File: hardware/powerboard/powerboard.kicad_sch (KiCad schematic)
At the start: 64 parts, among them J1 USB_B_Micro, J2 Boot, J3 Power, J4 SPI_0, J5 Debug, J6 SPI_1, J7 I2C_0, J8 I2C_1, J9 UART_0, SW1 Oct_Up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

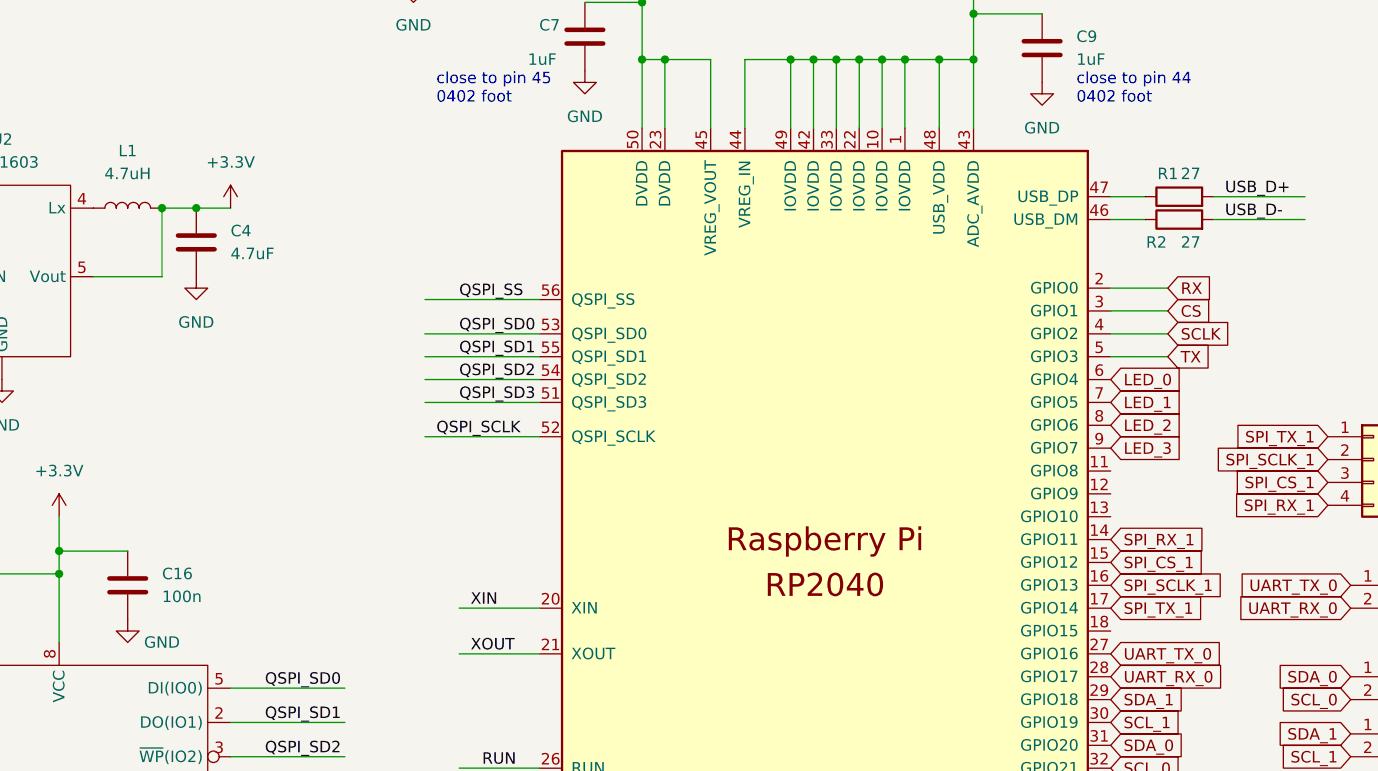
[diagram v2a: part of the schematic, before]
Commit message: GPIO Functions done Small footprint changes to powerboard
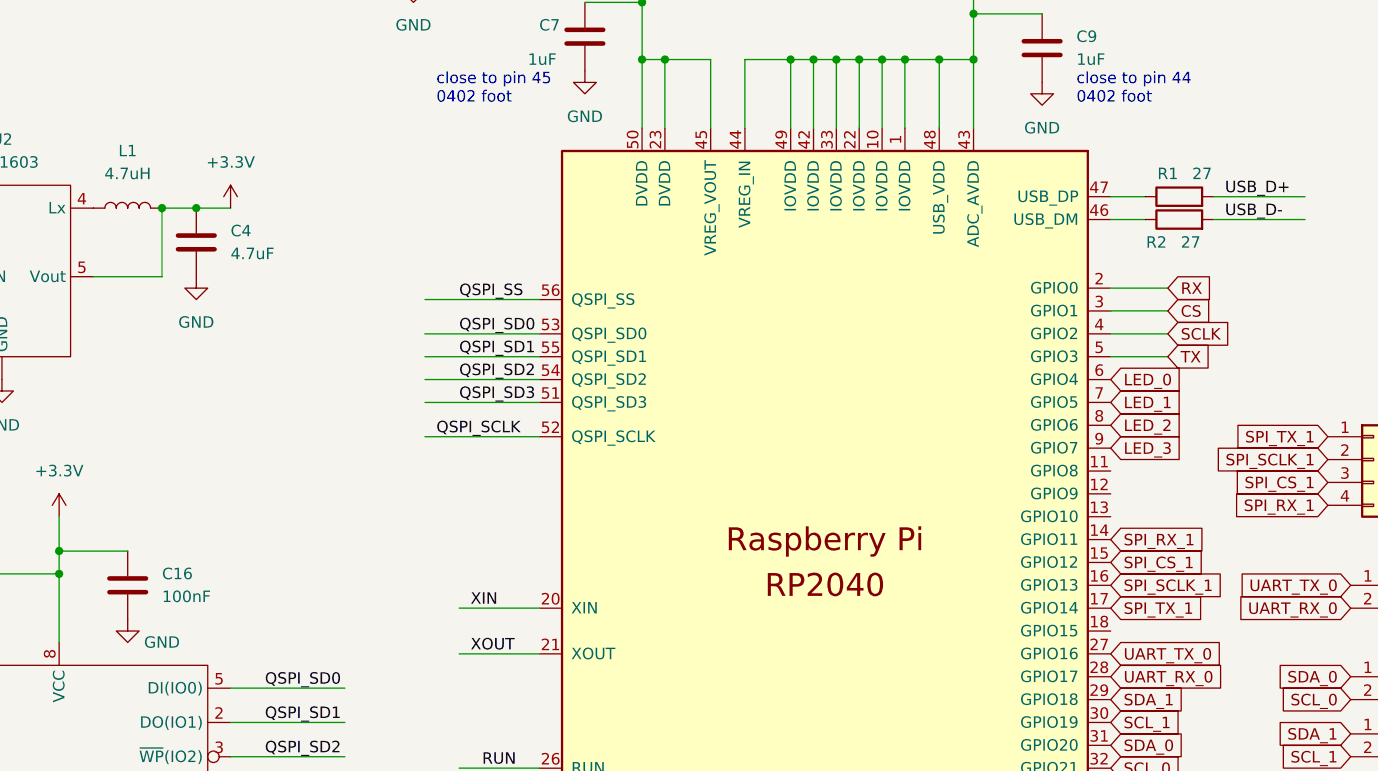
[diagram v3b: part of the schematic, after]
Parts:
- C16: value 100n -> 100nF
- C22: footprint Capacitor_SMD:C_0603_1608Metric -> Capacitor_SMD:C_0805_2012Metric
- C23, C24: footprint Capacitor_SMD:C_0603_1608Metric -> Capacitor_SMD:C_0402_1005Metric
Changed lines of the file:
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@@
     (in_bom yes) (on_board yes)
     (property "Reference" "R1" (id 0) (at 196.85 58.42 90))
-    (property "Value" "27" (id 1) (at 199.39 58.42 90))
+    (property "Value" "27" (id 1) (at 200.66 58.42 90))
     (property "Footprint" "Resistor_SMD:R_0402_1005Metric" (id 2) (at 198.12 62.738 90)
       (effects (font (size 1.27 1.27)) hide)
@@
       (effects (font (size 1.27 1.27)) (justify left))
     )
-    (property "Footprint" "Capacitor_SMD:C_0603_1608Metric" (id 2) (at 77.1652 194.31 0)
+    (property "Footprint" "Capacitor_SMD:C_0402_1005Metric" (id 2) (at 77.1652 194.31 0)
       (effects (font (size 1.27 1.27)) hide)
     )
@@
       (effects (font (size 1.27 1.27)) (justify left))
     )
-    (property "Value" "100n" (id 1) (at 85.09 105.4099 0)
+    (property "Value" "100nF" (id 1) (at 85.09 105.4099 0)
       (effects (font (size 1.27 1.27)) (justify left))
     )
@@
       (effects (font (size 1.27 1.27)) (justify left))
     )
-    (property "Footprint" "Capacitor_SMD:C_0603_1608Metric" (id 2) (at 87.3252 180.34 0)
+    (property "Footprint" "Capacitor_SMD:C_0402_1005Metric" (id 2) (at 87.3252 180.34 0)
       (effects (font (size 1.27 1.27)) hide)
     )
@@
       (effects (font (size 1.27 1.27)) (justify left))
     )
-    (property "Footprint" "Capacitor_SMD:C_0603_1608Metric" (id 2) (at 279.0952 67.31 0)
+    (property "Footprint" "Capacitor_SMD:C_0805_2012Metric" (id 2) (at 279.0952 67.31 0)
       (effects (font (size 1.27 1.27)) hide)
     )
@@
     )
     (path "/d94ce941-d973-4d50-9dcc-a718392ddb9d"
-      (reference "C16") (unit 1) (value "100n") (footprint "Capacitor_SMD:C_0603_1608Metric")
+      (reference "C16") (unit 1) (value "100nF") (footprint "Capacitor_SMD:C_0603_1608Metric")
     )
     (path "/17adefd0-27a9-46b5-ae61-8e173f9c410f"
@@
     )
     (path "/ea5ef4b8-1862-4679-b068-1d8aea36089c"
-      (reference "C22") (unit 1) (value "10u") (footprint "Capacitor_SMD:C_0603_1608Metric")
+      (reference "C22") (unit 1) (value "10u") (footprint "Capacitor_SMD:C_0805_2012Metric")
     )
     (path "/9cb838af-a4f1-4ad0-b52d-a490cbb33159"
-      (reference "C23") (unit 1) (value "100n") (footprint "Capacitor_SMD:C_0603_1608Metric")
+      (reference "C23") (unit 1) (value "100n") (footprint "Capacitor_SMD:C_0402_1005Metric")
     )
     (path "/e1581637-2922-404a-90ea-0fc41dfb0ff5"
-      (reference "C24") (unit 1) (value "100n") (footprint "Capacitor_SMD:C_0603_1608Metric")
+      (reference "C24") (unit 1) (value "100n") (footprint "Capacitor_SMD:C_0402_1005Metric")
     )
     (path "/f5fb7d56-553e-4b20-aeec-a8e1c9b6a666"

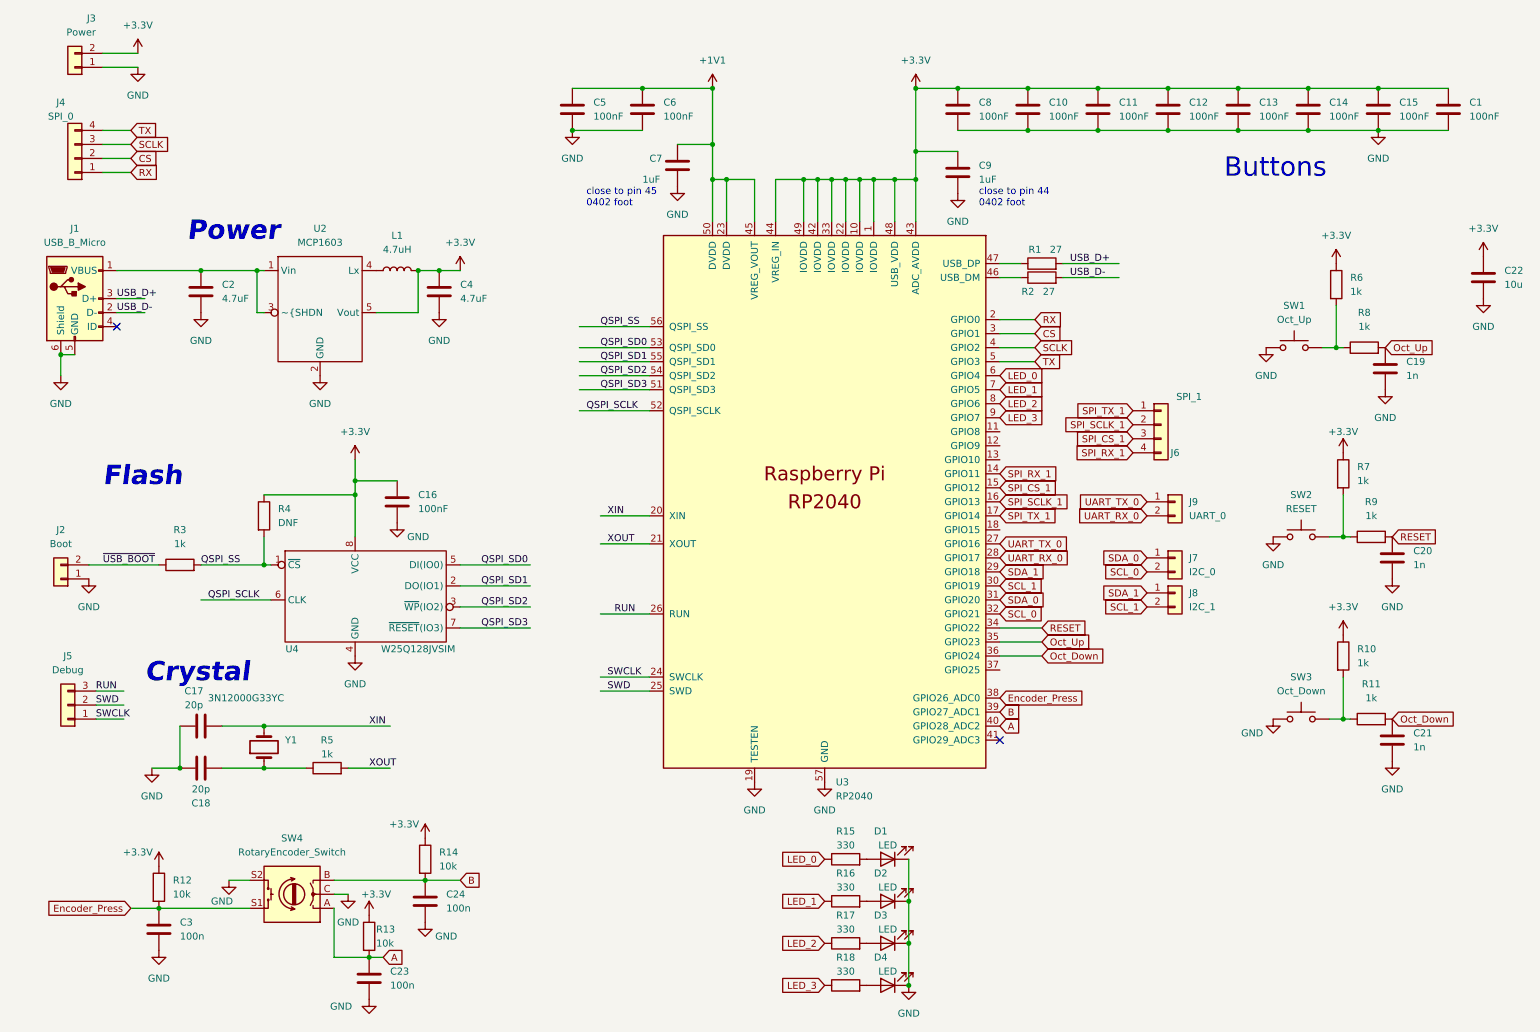
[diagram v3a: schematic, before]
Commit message: Powerboard Renovations (Stage 1 of Finalization)
Expand SPI 0 Header to match Display Header
Confirm footprints for passives
Power Circuit reorganized for short return paths
Reset button now toggles RUN pin, does not connect to GPIO
GPIO 10 connected to DISPLAY_RESET pin
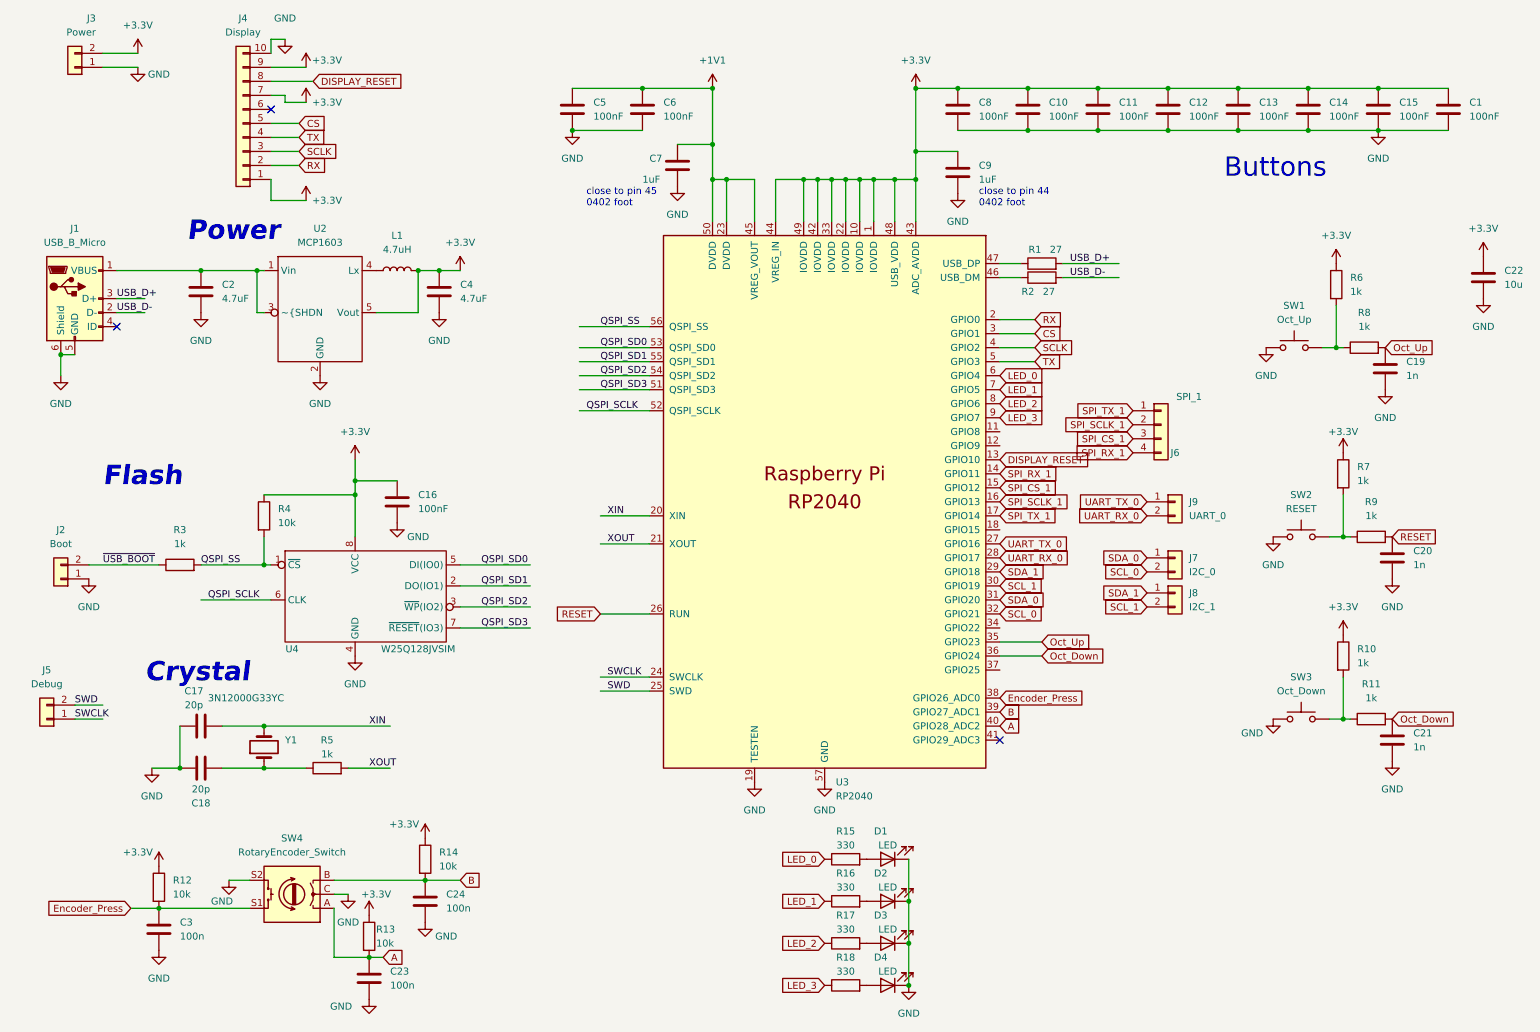
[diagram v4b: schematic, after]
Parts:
- removed J4: SPI_0, Connector_PinHeader_2.54mm:PinHeader_1x04_P2.54mm_Vertical, symbol Connector_Generic:Conn_01x04
- removed J5: Debug, Connector_PinHeader_2.54mm:PinHeader_1x03_P2.54mm_Vertical, symbol Connector_Generic:Conn_01x03
- added J4: Display, Connector_PinSocket_2.54mm:PinSocket_1x10_P2.54mm_Vertical, symbol Connector_Generic:Conn_01x10
- added J5: Debug, symbol Connector_Generic:Conn_01x02
- R4: value DNF -> 10k
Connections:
- net RUN is gone; now on net RESET: U3.26 (RUN)
- net +3.3V: now also J4.1 (Pin_1), J4.7 (Pin_7), J4.9 (Pin_9)
- net CS: now also J4.5 (Pin_5)
- net GND: now also J4.10 (Pin_10)
- net RESET: no longer U3.34 (GPIO22)
- net RX: now also J4.2 (Pin_2)
- net SCLK: now also J4.3 (Pin_3)
- net SWCLK: now also J5.1 (Pin_1)
- net SWD: now also J5.2 (Pin_2)
- net TX: now also J4.4 (Pin_4)
- net DISPLAY_RESET: now reaches U3.13 (GPIO10)
- net DISPLAY_RESET: now also J4.8 (Pin_8)
- no-connect marks 2 -> 3

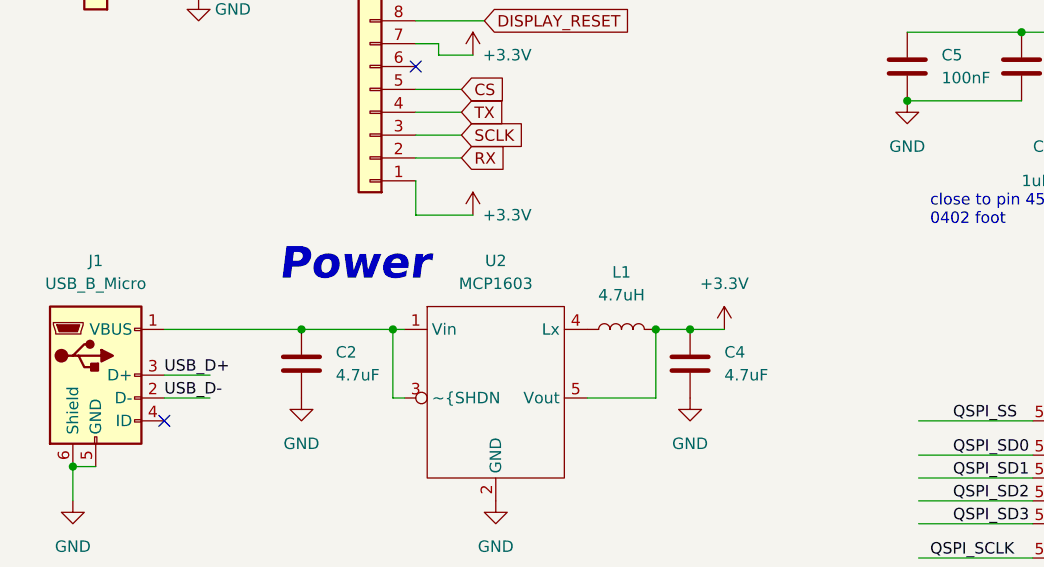
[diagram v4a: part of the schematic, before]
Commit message: Power Measurement Headers
Added, did not connect power measurement headers.
Do we need these?
How do we want to measure power?
This is a high current, high frequency path, can we even do a header like this?
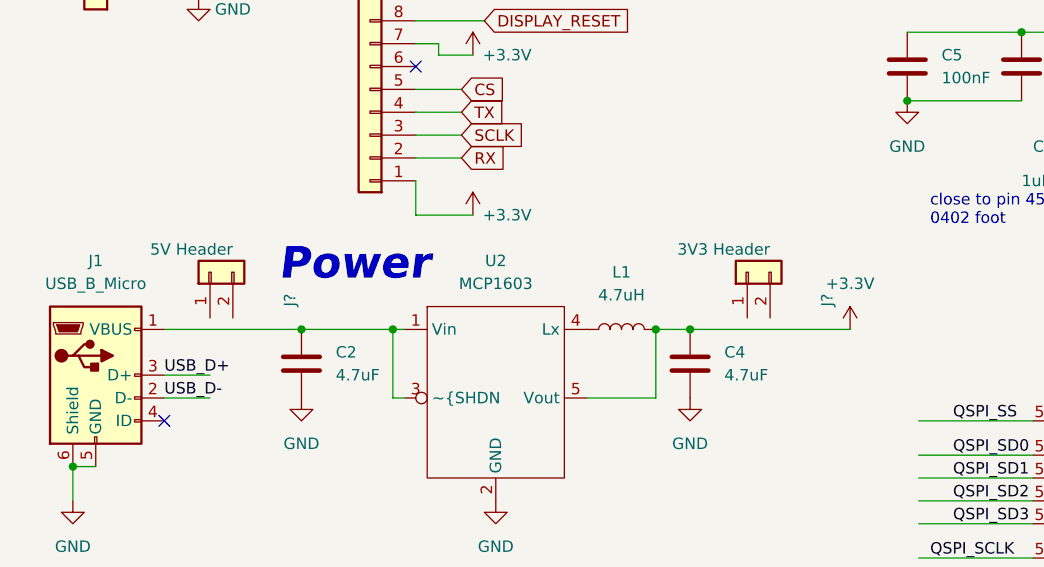
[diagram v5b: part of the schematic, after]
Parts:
- added J?: 5V Header, Connector_PinHeader_2.54mm:PinHeader_1x02_P2.54mm_Horizontal, symbol Connector_Generic:Conn_01x02
- added J?: 3V3 Header, Connector_PinHeader_2.54mm:PinHeader_1x02_P2.54mm_Horizontal, symbol Connector_Generic:Conn_01x02
- J5: footprint (none) -> Connector_PinSocket_2.54mm:PinSocket_1x02_P2.54mm_Vertical
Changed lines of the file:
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@@
     (stroke (width 0) (type default) (color 0 0 0 0))
   )
-  (wire (pts (xy 88.9 62.23) (xy 92.71 62.23))
+  (wire (pts (xy 88.9 62.23) (xy 106.68 62.23))
     (stroke (width 0) (type default) (color 0 0 0 0))
   )
@@
     (pin "2")
   )
+  (symbol (lib_id "Connector_Generic:Conn_01x02") (at 35.56 55.88 90) (unit 1)
+    (in_bom yes) (on_board yes)
+    (property "Reference" "J?" (id 0) (at 44.45 59.69 0)
+      (effects (font (size 1.27 1.27)) (justify left))
+    )
+    (property "Value" "5V Header" (id 1) (at 38.1 53.34 90)
+      (effects (font (size 1.27 1.27)) (justify left))
+    )
+    (property "Footprint" "Connector_PinHeader_2.54mm:PinHeader_1x02_P2.54mm_Horizontal" (id 2) (at 35.56 55.88 0)
+      (effects (font (size 1.27 1.27)) hide)
+    )
+    (property "Datasheet" "~" (id 3) (at 35.56 55.88 0)
+      (effects (font (size 1.27 1.27)) hide)
+    )
+    (pin "1")
+    (pin "2")
+  )
   (symbol (lib_id "Device:LED") (at 170.18 184.15 180) (unit 1)
     (in_bom yes) (on_board yes)
@@
     (pin "1")
   )
+  (symbol (lib_id "Connector_Generic:Conn_01x02") (at 95.25 55.88 90) (unit 1)
+    (in_bom yes) (on_board yes)
+    (property "Reference" "J?" (id 0) (at 104.14 59.69 0)
+      (effects (font (size 1.27 1.27)) (justify left))
+    )
+    (property "Value" "3V3 Header" (id 1) (at 97.79 53.34 90)
+      (effects (font (size 1.27 1.27)) (justify left))
+    )
+    (property "Footprint" "Connector_PinHeader_2.54mm:PinHeader_1x02_P2.54mm_Horizontal" (id 2) (at 95.25 55.88 0)
+      (effects (font (size 1.27 1.27)) hide)
+    )
+    (property "Datasheet" "~" (id 3) (at 95.25 55.88 0)
+      (effects (font (size 1.27 1.27)) hide)
+    )
+    (pin "1")
+    (pin "2")
+  )
   (symbol (lib_id "Device:R") (at 86.36 168.91 0) (unit 1)
     (in_bom yes) (on_board yes) (fields_autoplaced)
@@
     (property "Reference" "J5" (id 0) (at 17.78 134.62 0))
     (property "Value" "Debug" (id 1) (at 17.78 137.16 0))
-    (property "Footprint" "" (id 2) (at 17.78 143.51 0)
+    (property "Footprint" "Connector_PinSocket_2.54mm:PinSocket_1x02_P2.54mm_Vertical" (id 2) (at 17.78 143.51 0)
       (effects (font (size 1.27 1.27)) hide)
     )
@@
     (pin "2")
   )
-  (symbol (lib_id "power:+3.3V") (at 92.71 62.23 0) (unit 1)
-    (in_bom yes) (on_board yes) (fields_autoplaced)
-    (property "Reference" "#PWR011" (id 0) (at 92.71 66.04 0)
-      (effects (font (size 1.27 1.27)) hide)
-    )
-    (property "Value" "+3.3V" (id 1) (at 92.71 57.15 0))
-    (property "Footprint" "" (id 2) (at 92.71 62.23 0)
-      (effects (font (size 1.27 1.27)) hide)
-    )
-    (property "Datasheet" "" (id 3) (at 92.71 62.23 0)
+  (symbol (lib_id "power:+3.3V") (at 106.68 62.23 0) (unit 1)
+    (in_bom yes) (on_board yes) (fields_autoplaced)
+    (property "Reference" "#PWR011" (id 0) (at 106.68 66.04 0)
+      (effects (font (size 1.27 1.27)) hide)
+    )
+    (property "Value" "+3.3V" (id 1) (at 106.68 57.15 0))
+    (property "Footprint" "" (id 2) (at 106.68 62.23 0)
+      (effects (font (size 1.27 1.27)) hide)
+    )
+    (property "Datasheet" "" (id 3) (at 106.68 62.23 0)
       (effects (font (size 1.27 1.27)) hide)
     )
@@
       (reference "J9") (unit 1) (value "UART_0") (footprint "Connector_PinHeader_2.54mm:PinHeader_1x02_P2.54mm_Vertical")
     )
+    (path "/85a4f74c-0515-4fc6-8537-31474813c8f4"
+      (reference "J?") (unit 1) (value "5V Header") (footprint "Connector_PinHeader_2.54mm:PinHeader_1x02_P2.54mm_Horizontal")
+    )
+    (path "/92b480d2-b732-4893-9180-b4065c6eff21"
+      (reference "J?") (unit 1) (value "3V3 Header") (footprint "Connector_PinHeader_2.54mm:PinHeader_1x02_P2.54mm_Horizontal")
+    )
     (path "/985ac95d-4079-4633-83a9-2b6fdcd0332b"
